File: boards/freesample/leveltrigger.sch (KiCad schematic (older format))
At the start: 23 parts, among them U10 PI6C59S6005, U9 HMC675LP3E

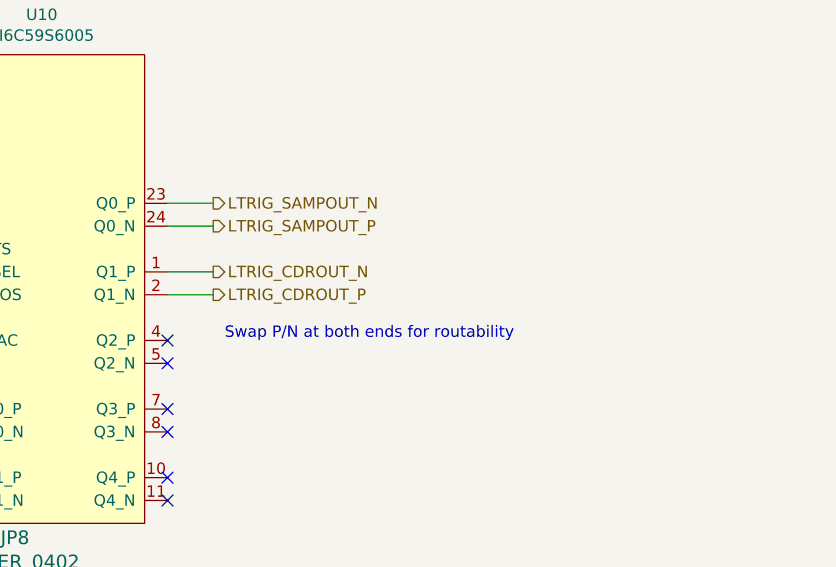
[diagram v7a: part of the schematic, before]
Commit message: Continued layout on level trigger subsystem
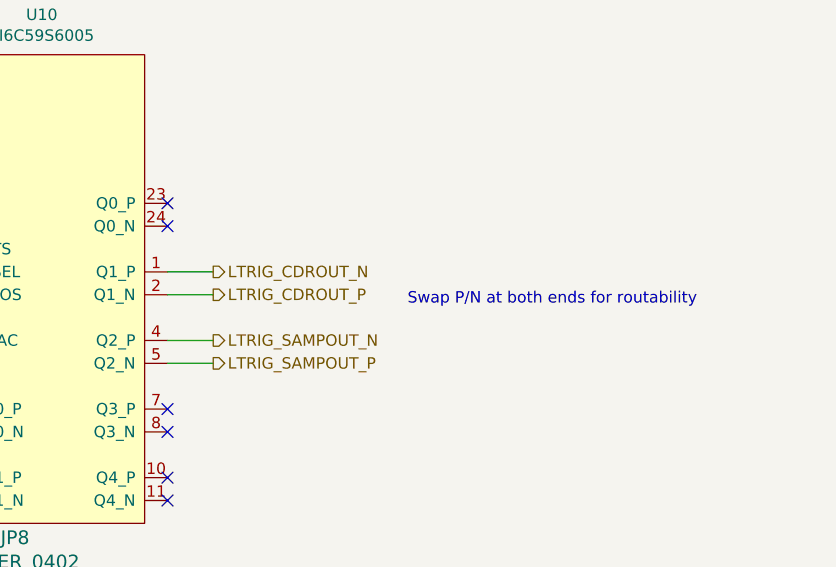
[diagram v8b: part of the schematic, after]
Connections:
- net LTRIG_SAMPOUT_N: now also U10.4 (Q2_P); no longer U10.23 (Q0_P)
- net LTRIG_SAMPOUT_P: now also U10.5 (Q2_N); no longer U10.24 (Q0_N)
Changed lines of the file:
@@
 Text HLabel 3750 3000 0    50   Input ~ 0
 LTRIG_DIN
-Text HLabel 8850 2450 2    50   Output ~ 0
-LTRIG_CDROUT_P
-Text HLabel 8850 2350 2    50   Output ~ 0
-LTRIG_CDROUT_N
 Text HLabel 3750 1800 0    50   Input ~ 0
 3V3
@@
 Text HLabel 3750 3100 0    50   Input ~ 0
 LTRIG_VT
-Text HLabel 8850 2150 2    50   Output ~ 0
+Text HLabel 8850 2750 2    50   Output ~ 0
 LTRIG_SAMPOUT_P
-Text HLabel 8850 2050 2    50   Output ~ 0
+Text HLabel 8850 2650 2    50   Output ~ 0
 LTRIG_SAMPOUT_N
 $Comp
@@
 	7400 1950 7550 1950
 Wire Wire Line
-	8850 2050 8650 2050
-Wire Wire Line
-	8650 2150 8850 2150
-NoConn ~ 8650 2650
-NoConn ~ 8650 2750
+	8850 2650 8650 2650
+Wire Wire Line
+	8650 2750 8850 2750
 NoConn ~ 8650 2950
 NoConn ~ 8650 3050
 NoConn ~ 8650 3250
 NoConn ~ 8650 3350
-Wire Wire Line
-	8850 2350 8650 2350
-Wire Wire Line
-	8650 2450 8850 2450
 Text Notes 4950 2600 0    50   ~ 0
 Common mode is VCCO-0.15 = 1.65V\nVout = 1.8 to 1.5, 300 mV differential
@@
 Text Label 7550 3050 2    50   ~ 0
 LTRIG_AC_P
-Text Notes 8900 2650 0    50   ~ 0
+Text Notes 9700 2500 0    50   ~ 0
 Swap P/N at both ends for routability
+Wire Wire Line
+	8650 2450 8850 2450
+Wire Wire Line
+	8850 2350 8650 2350
+Text HLabel 8850 2350 2    50   Output ~ 0
+LTRIG_CDROUT_N
+Text HLabel 8850 2450 2    50   Output ~ 0
+LTRIG_CDROUT_P
+NoConn ~ 8650 2150
+NoConn ~ 8650 2050
 $EndSCHEMATC
